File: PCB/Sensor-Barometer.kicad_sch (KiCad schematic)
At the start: 0 parts

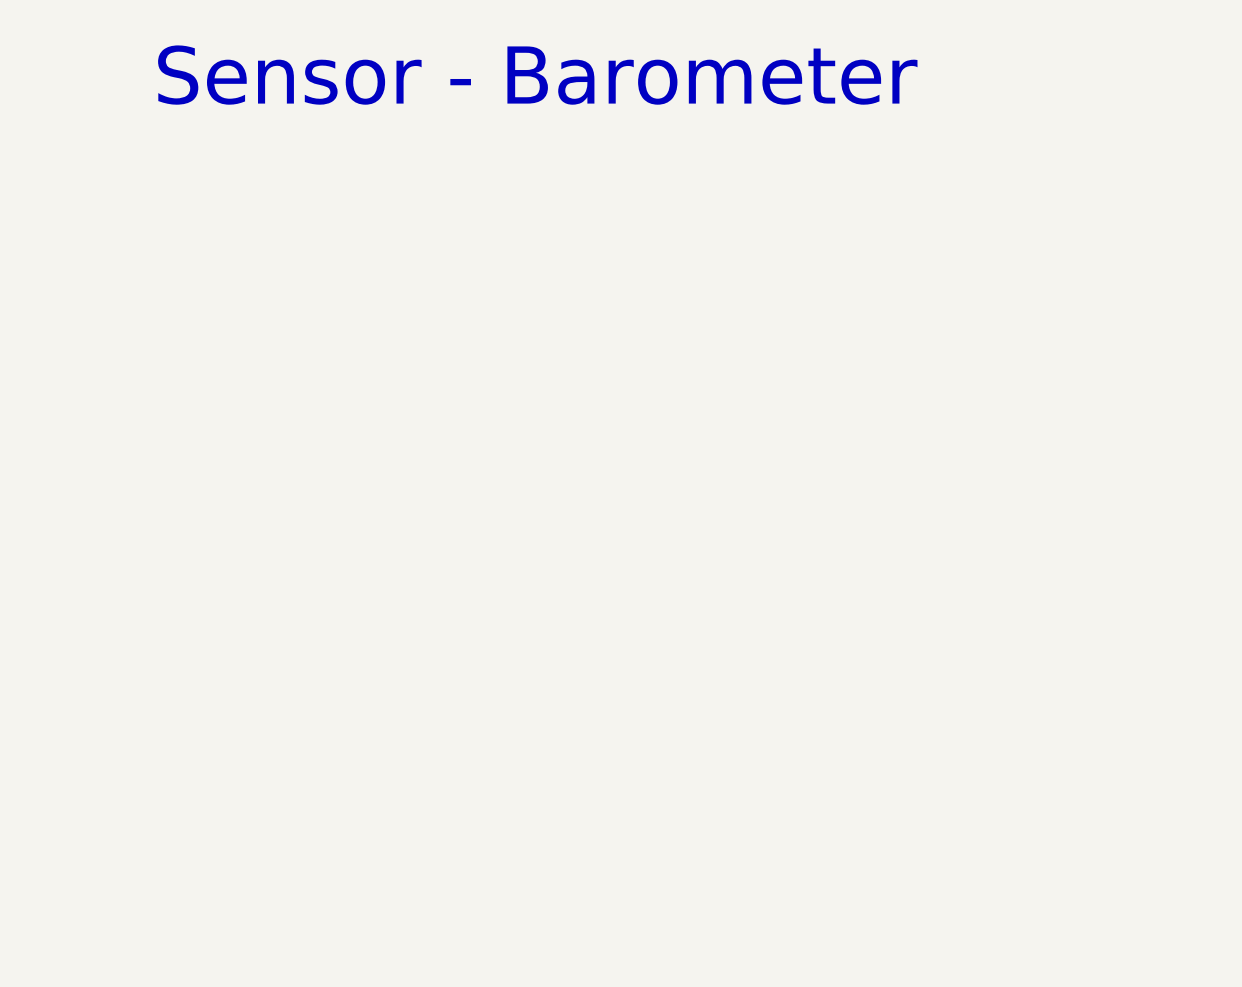
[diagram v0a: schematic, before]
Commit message: Added Barometer and Started External Sensors
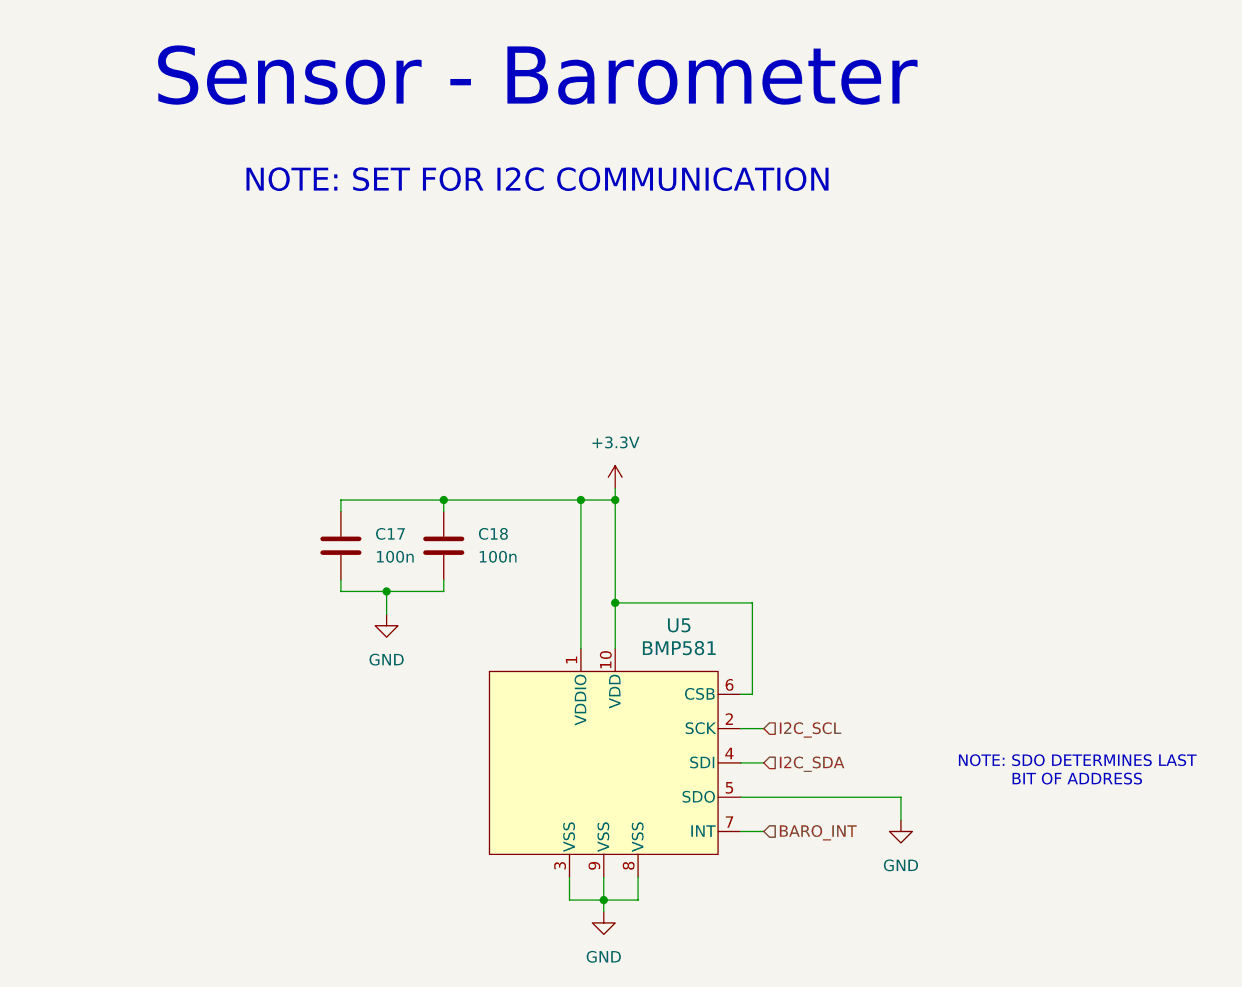
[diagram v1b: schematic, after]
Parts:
- added C17, C18: 100n, Capacitor_SMD:C_0402_1005Metric, symbol Device:C
- added U5: BMP581, QFN10_BMP581_BOS, symbol Sensors_Custom:BMP581
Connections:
- new net +3.3V: C17.1, C18.1, U5.1 (VDDIO), U5.10 (VDD), U5.6 (CSB)
- new net BARO_INT: U5.7 (INT)
- new net GND: C17.2, C18.2, U5.3 (VSS), U5.5 (SDO), U5.8 (VSS), U5.9 (VSS)
- new net I2C_SCL: U5.2 (SCK)
- new net I2C_SDA: U5.4 (SDI)
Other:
- note added: "NOTE: SDO DETERMINES LAST BIT OF ADDRESS"
- note added: "NOTE: SET FOR I2C COMMUNICATION"
